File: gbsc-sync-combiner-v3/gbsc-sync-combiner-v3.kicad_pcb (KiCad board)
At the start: 2 copper layers, 33 x 48 mm, 14 parts, among them J1 DB15_Female_HighDensity_Mount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, J2 JST-XH, J3 JST-XH, U1 74LS86

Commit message: minor adjustment
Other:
- board text added: "GBS-C Sync Combiner v1.3 c. 01/2022 Details on Github: Softdrink117/gbsc-sync-combiner CERN-OHL-W"
- board text removed: "GBS-C Sync Combiner v1.0 c. 11/2021 Details on Github: Softdrink117/gbsc-sync-combiner CERN-OHL-W"
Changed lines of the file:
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@@
     (effects (font (size 0.4572 0.4572) (thickness 0.0762)) (justify left))
   )
-  (gr_text "GBS-C Sync Combiner \nv1.0 c. 11/2021\nDetails on Github:\nSoftdrink117/gbsc-sync-combiner\nCERN-OHL-W" (at 109.5 93) (layer "F.SilkS")
+  (gr_text "GBS-C Sync Combiner \nv1.3 c. 01/2022\nDetails on Github:\nSoftdrink117/gbsc-sync-combiner\nCERN-OHL-W" (at 109.5 93) (layer "F.SilkS")
     (effects (font (size 0.4572 0.4572) (thickness 0.0762)) (justify left))
   )
@@
   )
   (segment (start 109.793312 81.043312) (end 117.293312 73.543312) (width 0.381) (layer "F.Cu") (net 1))
-  (segment (start 107 64.75) (end 107 62) (width 0.381) (layer "F.Cu") (net 1))
   (segment (start 110 87) (end 117.396447 87) (width 0.381) (layer "F.Cu") (net 1))
   (segment (start 108.362605 79.194999) (end 102.906659 79.194999) (width 0.381) (layer "F.Cu") (net 1))
@@
   (segment (start 121.644511 72.144511) (end 121.644511 56.644511) (width 0.381) (layer "F.Cu") (net 1))
   (segment (start 110 61.5) (end 110 59) (width 0.381) (layer "F.Cu") (net 1))
+  (segment (start 107 64.75) (end 107 62.75) (width 0.381) (layer "F.Cu") (net 1))
   (segment (start 102.10666 76.105) (end 102.10666 78.395) (width 0.381) (layer "F.Cu") (net 1))
   (segment (start 110.916833 61.5) (end 110 61.5) (width 0.381) (layer "F.Cu") (net 1))
   (segment (start 118.603553 87.5) (end 120 87.5) (width 0.381) (layer "F.Cu") (net 1))
-  (segment (start 107.5 61.5) (end 110 61.5) (width 0.381) (layer "F.Cu") (net 1))
   (segment (start 120 84.24) (end 120 87.5) (width 0.381) (layer "F.Cu") (net 1))
   (segment (start 111.505971 61.744029) (end 117.421136 67.659194) (width 0.381) (layer "F.Cu") (net 1))
@@
   (segment (start 108.60949 85.057226) (end 108.60949 83.14051) (width 0.381) (layer "F.Cu") (net 1))
   (segment (start 102.10666 73.815) (end 102.10666 76.105) (width 0.381) (layer "F.Cu") (net 1))
+  (segment (start 108.25 61.5) (end 110 61.5) (width 0.381) (layer "F.Cu") (net 1))
   (segment (start 110 55.853553) (end 110 59) (width 0.381) (layer "F.Cu") (net 1))
   (segment (start 118.871756 72.889499) (end 120.899523 72.889499) (width 0.381) (layer "F.Cu") (net 1))
@@
   (arc (start 109.75 55.25) (mid 109.935027 55.526912) (end 110 55.853553) (width 0.381) (layer "F.Cu") (net 1))
   (arc (start 109 86) (mid 108.710981 85.567452) (end 108.60949 85.057226) (width 0.381) (layer "F.Cu") (net 1))
-  (arc (start 107 62) (mid 107.146447 61.646447) (end 107.5 61.5) (width 0.381) (layer "F.Cu") (net 1))
   (arc (start 110.36541 78.36541) (mid 109.446515 78.979396) (end 108.362605 79.194999) (width 0.381) (layer "F.Cu") (net 1))
+  (arc (start 107 62.75) (mid 107.366117 61.866117) (end 108.25 61.5) (width 0.381) (layer "F.Cu") (net 1))
   (arc (start 117.293312 73.543312) (mid 118.017507 73.05942) (end 118.871756 72.889499) (width 0.381) (layer "F.Cu") (net 1))
   (segment (start 127.62 71.54) (end 127.62 74.08) (width 0.381) (layer "F.Cu") (net 2))
@@
   (arc (start 105.896447 77.25) (mid 106.223087 77.185028) (end 106.5 77) (width 0.254) (layer "F.Cu") (net 13))
   (arc (start 106.5 77) (mid 107.053825 76.629946) (end 107.707106 76.5) (width 0.254) (layer "F.Cu") (net 13))
-  (segment (start 115.103553 68.5) (end 116.5 68.5) (width 0.254) (layer "F.Cu") (net 15))
-  (segment (start 110 69) (end 113.896447 69) (width 0.254) (layer "F.Cu") (net 15))
-  (arc (start 114.5 68.75) (mid 114.776912 68.564973) (end 115.103553 68.5) (width 0.254) (layer "F.Cu") (net 15))
-  (arc (start 113.896447 69) (mid 114.223087 68.935028) (end 114.5 68.75) (width 0.254) (layer "F.Cu") (net 15))
+  (segment (start 113.103553 68.5) (end 116.5 68.5) (width 0.254) (layer "F.Cu") (net 15))
+  (segment (start 110 69) (end 111.896447 69) (width 0.254) (layer "F.Cu") (net 15))
+  (arc (start 112.5 68.75) (mid 112.776912 68.564973) (end 113.103553 68.5) (width 0.254) (layer "F.Cu") (net 15))
+  (arc (start 111.896447 69) (mid 112.223087 68.935028) (end 112.5 68.75) (width 0.254) (layer "F.Cu") (net 15))
   (segment (start 116.5 80.25) (end 116.5 78.66) (width 0.254) (layer "F.Cu") (net 16))
   (segment (start 120 81.7) (end 117.95 81.7) (width 0.254) (layer "F.Cu") (net 16))

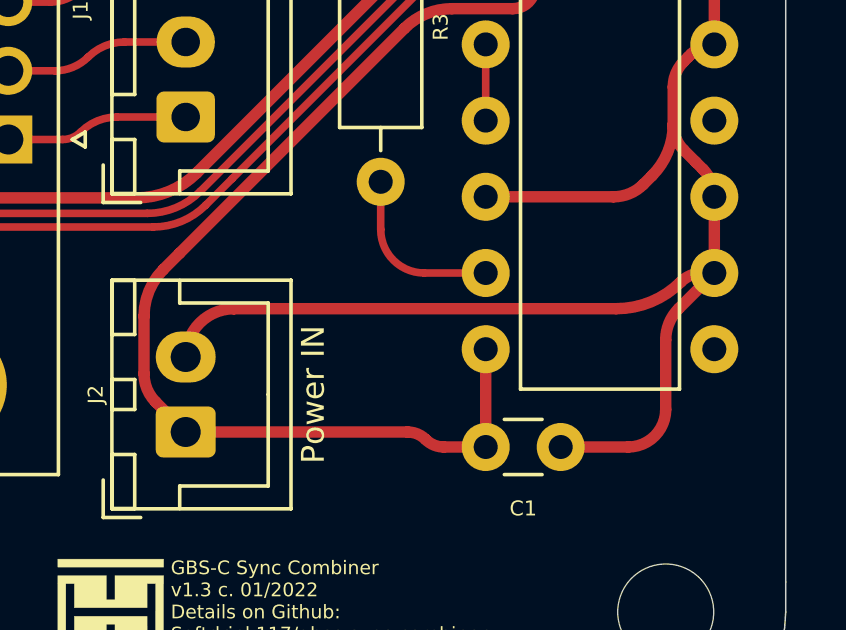
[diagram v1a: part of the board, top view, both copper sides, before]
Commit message: Edited gitignore, minor board adjustments
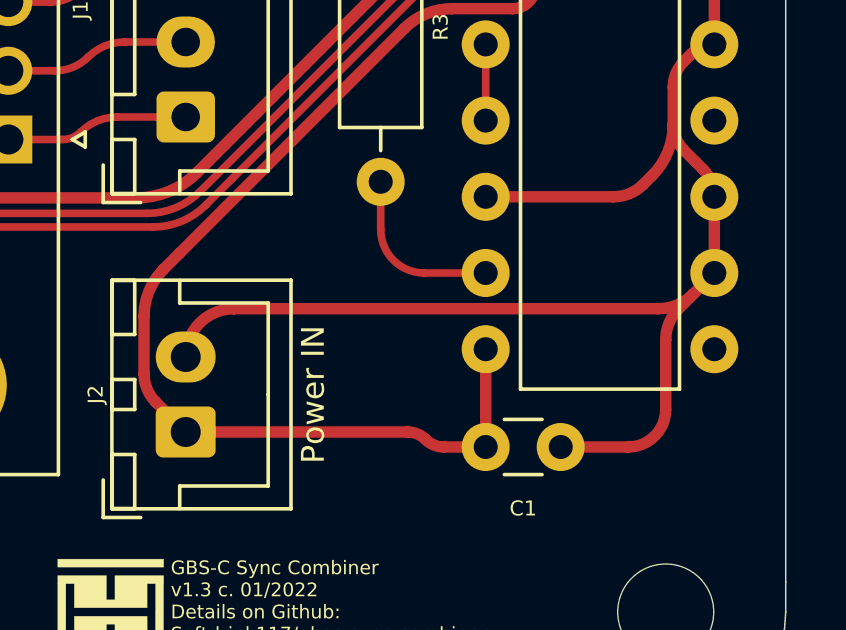
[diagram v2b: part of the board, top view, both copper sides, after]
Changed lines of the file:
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@@
   (segment (start 127.62 71.54) (end 127.62 74.08) (width 0.381) (layer "F.Cu") (net 2))
   (segment (start 126.603553 74.646446) (end 126.75 74.5) (width 0.381) (layer "F.Cu") (net 2))
-  (segment (start 127.62 81.7) (end 126.429499 82.890501) (width 0.381) (layer "F.Cu") (net 2))
   (segment (start 127 78) (end 126.603554 77.603554) (width 0.381) (layer "F.Cu") (net 2))
   (segment (start 127.66 58.5) (end 127.66 62.5) (width 0.381) (layer "F.Cu") (net 2))
@@
   (segment (start 122.5 87.5) (end 124.75 87.5) (width 0.381) (layer "F.Cu") (net 2))
   (segment (start 120 79.16) (end 124.260173 79.16) (width 0.381) (layer "F.Cu") (net 2))
+  (segment (start 111.609499 82.890501) (end 111.609989 82.890011) (width 0.381) (layer "F.Cu") (net 2))
   (segment (start 127.66 68.96) (end 127.62 69) (width 0.381) (layer "F.Cu") (net 2))
   (segment (start 127.224264 81.7) (end 127.62 81.7) (width 0.381) (layer "F.Cu") (net 2))
+  (segment (start 127.62 81.7) (end 126.91 82.41) (width 0.381) (layer "F.Cu") (net 2))
   (segment (start 126.75 74.5) (end 126.851801 74.398199) (width 0.381) (layer "F.Cu") (net 2))
+  (segment (start 111.609989 82.890011) (end 125.751151 82.890011) (width 0.381) (layer "F.Cu") (net 2))
   (segment (start 126.25 76.75) (end 126.25 75.5) (width 0.381) (layer "F.Cu") (net 2))
-  (segment (start 111.609989 82.890011) (end 124.351324 82.890011) (width 0.381) (layer "F.Cu") (net 2))
+  (segment (start 126.91 82.41) (end 126.429499 82.890501) (width 0.381) (layer "F.Cu") (net 2))
   (segment (start 127.62 79.16) (end 127.62 81.7) (width 0.381) (layer "F.Cu") (net 2))
   (segment (start 127.238162 78.238163) (end 127 78) (width 0.381) (layer "F.Cu") (net 2))
-  (segment (start 111.609499 82.890501) (end 111.609989 82.890011) (width 0.381) (layer "F.Cu") (net 2))
   (segment (start 125.25 78.75) (end 125.542893 78.457107) (width 0.381) (layer "F.Cu") (net 2))
   (segment (start 127.66 62.5) (end 127.66 68.96) (width 0.381) (layer "F.Cu") (net 2))
-  (arc (start 111.609499 82.890501) (mid 110.471411 83.361912) (end 110 84.5) (width 0.381) (layer "F.Cu") (net 2))
   (arc (start 126.851801 74.398199) (mid 127.204253 74.162698) (end 127.62 74.08) (width 0.381) (layer "F.Cu") (net 2))
   (arc (start 126 83.927403) (mid 126.111623 83.366236) (end 126.429499 82.890501) (width 0.381) (layer "F.Cu") (net 2))
+  (arc (start 125.751151 82.890011) (mid 126.378315 82.765261) (end 126.91 82.41) (width 0.381) (layer "F.Cu") (net 2))
   (arc (start 126.603554 77.603554) (mid 126.341886 77.21194) (end 126.25 76.75) (width 0.381) (layer "F.Cu") (net 2))
+  (arc (start 110 84.5) (mid 110.471411 83.361912) (end 111.609499 82.890501) (width 0.381) (layer "F.Cu") (net 2))
   (arc (start 127.62 79.16) (mid 127.520764 78.661105) (end 127.238162 78.238163) (width 0.381) (layer "F.Cu") (net 2))
   (arc (start 126.25 75.5) (mid 126.341886 75.03806) (end 126.603553 74.646446) (width 0.381) (layer "F.Cu") (net 2))
   (arc (start 124.260173 79.16) (mid 124.795863 79.053445) (end 125.25 78.75) (width 0.381) (layer "F.Cu") (net 2))
-  (arc (start 126.5 82) (mid 126.832294 81.777968) (end 127.224264 81.7) (width 0.381) (layer "F.Cu") (net 2))
   (arc (start 124.75 87.5) (mid 125.633883 87.133883) (end 126 86.25) (width 0.381) (layer "F.Cu") (net 2))
   (arc (start 125.542893 78.457107) (mid 126.066229 77.67388) (end 126.25 76.75) (width 0.381) (layer "F.Cu") (net 2))
-  (arc (start 124.351324 82.890011) (mid 125.514179 82.658705) (end 126.5 82) (width 0.381) (layer "F.Cu") (net 2))
   (arc (start 127.54 74) (mid 127.596569 74.023431) (end 127.62 74.08) (width 0.381) (layer "F.Cu") (net 2))
   (segment (start 102.03666 60.435) (end 97.873593 64.598067) (width 0.381) (layer "F.Cu") (net 3))

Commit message: Major updates
- Updated v1.3 PCB design
- Created README
- Created BOM
- Created gerbers
- Sent gerbers to fab
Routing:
- net /HSync: track 46.6 -> 45.1 mm
- net +5V: track 59.8 -> 59.2 mm
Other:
- board text added: "GBS-C Sync Combiner v1.3 c. 01/2022 Design by Softdrink 117 Details on Github: Softdrink117/gbsc-sync-combiner"
- board text removed: "GBS-C Sync Combiner v1.3 c. 01/2022 Details on Github: Softdrink117/gbsc-sync-combiner CERN-OHL-W"
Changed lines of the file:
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@@
     (pad_to_mask_clearance 0)
     (pcbplotparams
-      (layerselection 0x00010fc_ffffffff)
+      (layerselection 0x00010f0_ffffffff)
       (disableapertmacros false)
       (usegerberextensions false)
@@
       (outputformat 1)
       (mirror false)
-      (drillshape 1)
+      (drillshape 0)
       (scaleselection 1)
-      (outputdirectory "")
+      (outputdirectory "gerber/")
     )
   )
@@
     (fp_line (start -2.45 -2.35) (end -2.45 3.4) (layer "F.Fab") (width 0.1))
     (fp_line (start -0.625 -2.35) (end 0 -1.35) (layer "F.Fab") (width 0.1))
-    (pad "1" thru_hole roundrect locked (at 0 0 90) (size 1.7 2) (drill 1) (layers *.Cu *.Mask) (roundrect_rratio 0.147059)
+    (pad "1" thru_hole roundrect locked (at 0 0 90) (size 1.7 2) (drill 1) (layers *.Cu *.Mask) (roundrect_rratio 0.1470588235)
       (net 1 "GND"))
     (pad "2" thru_hole oval locked (at 2.5 0 90) (size 1.7 2) (drill 1) (layers *.Cu *.Mask)
@@
     (fp_line (start 19.95 -2.35) (end -2.45 -2.35) (layer "F.Fab") (width 0.1))
     (fp_line (start -2.45 3.4) (end 19.95 3.4) (layer "F.Fab") (width 0.1))
-    (pad "1" thru_hole roundrect locked (at 0 0 90) (size 1.7 1.95) (drill 0.95) (layers *.Cu *.Mask) (roundrect_rratio 0.147059)
+    (pad "1" thru_hole roundrect locked (at 0 0 90) (size 1.7 1.95) (drill 0.95) (layers *.Cu *.Mask) (roundrect_rratio 0.1470588235)
       (net 13 "Red"))
     (pad "2" thru_hole oval locked (at 2.5 0 90) (size 1.7 1.95) (drill 0.95) (layers *.Cu *.Mask)
@@
   (gr_poly
     (pts
-      (xy 109.5 54)
-      (xy 108.5 54)
-      (xy 108.5 53)
-      (xy 109.5 53)
+      (xy 109.05 54)
+      (xy 108.6 54)
+      (xy 108.6 53)
+      (xy 109.05 53)
     ) (layer "F.Mask") (width 0.1) (fill solid))
   (gr_line (start 101 49) (end 102 49) (layer "Edge.Cuts") (width 0.05))
@@
     (effects (font (size 0.4572 0.4572) (thickness 0.0762)) (justify left))
   )
-  (gr_text "GBS-C Sync Combiner \nv1.3 c. 01/2022\nDetails on Github:\nSoftdrink117/gbsc-sync-combiner\nCERN-OHL-W" (at 109.5 93) (layer "F.SilkS")
+  (gr_text "GBS-C Sync Combiner \nv1.3 c. 01/2022\nDesign by Softdrink 117\nDetails on Github:\nSoftdrink117/gbsc-sync-combiner" (at 109.50001 92.999992) (layer "F.SilkS")
     (effects (font (size 0.4572 0.4572) (thickness 0.0762)) (justify left))
   )
@@
   (segment (start 111.609499 82.890501) (end 111.609989 82.890011) (width 0.381) (layer "F.Cu") (net 2))
   (segment (start 127.66 68.96) (end 127.62 69) (width 0.381) (layer "F.Cu") (net 2))
-  (segment (start 127.224264 81.7) (end 127.62 81.7) (width 0.381) (layer "F.Cu") (net 2))
   (segment (start 127.62 81.7) (end 126.91 82.41) (width 0.381) (layer "F.Cu") (net 2))
   (segment (start 126.75 74.5) (end 126.851801 74.398199) (width 0.381) (layer "F.Cu") (net 2))
@@
   (arc (start 124.75 87.5) (mid 125.633883 87.133883) (end 126 86.25) (width 0.381) (layer "F.Cu") (net 2))
   (arc (start 125.542893 78.457107) (mid 126.066229 77.67388) (end 126.25 76.75) (width 0.381) (layer "F.Cu") (net 2))
-  (arc (start 127.54 74) (mid 127.596569 74.023431) (end 127.62 74.08) (width 0.381) (layer "F.Cu") (net 2))
   (segment (start 102.03666 60.435) (end 97.873593 64.598067) (width 0.381) (layer "F.Cu") (net 3))
-  (segment (start 102.03666 85.435) (end 101.935 85.435) (width 0.381) (layer "F.Cu") (net 3))
   (segment (start 97.5 65.5) (end 97.5 80.792894) (width 0.381) (layer "F.Cu") (net 3))
   (segment (start 102.03666 60.435) (end 107.654354 54.817306) (width 0.381) (layer "F.Cu") (net 3))
   (segment (start 98 82) (end 101.009562 85.009562) (width 0.381) (layer "F.Cu") (net 3))
-  (arc (start 102.01662 60.48338) (mid 102.031452 60.461183) (end 102.03666 60.435) (width 0.381) (layer "F.Cu") (net 3))
   (arc (start 107.654354 54.817306) (mid 108.058191 54.212922) (end 108.2 53.5) (width 0.381) (layer "F.Cu") (net 3))
   (arc (start 97.873593 64.598067) (mid 97.597094 65.011877) (end 97.5 65.5) (width 0.381) (layer "F.Cu") (net 3))
@@
   (segment (start 116 64.43934) (end 116 64.25) (width 0.254) (layer "F.Cu") (net 6))
   (segment (start 118.246905 68.246905) (end 118.246905 69.003095) (width 0.254) (layer "F.Cu") (net 6))
-  (segment (start 120 69) (end 119.5 69) (width 0.254) (layer "F.Cu") (net 6))
   (segment (start 118.246905 70.746905) (end 118.246905 69.003095) (width 0.254) (layer "F.Cu") (net 6))
-  (segment (start 120 69) (end 120 69.462689) (width 0.254) (layer "F.Cu") (net 6))
   (segment (start 110.481344 78.981344) (end 117.915358 71.54733) (width 0.254) (layer "F.Cu") (net 6))
   (segment (start 98.82056 73.9761) (end 100.12666 72.67) (width 0.254) (layer "F.Cu") (net 6))
@@
   (segment (start 118.246905 69.003095) (end 119.996905 69.003095) (width 0.254) (layer "F.Cu") (net 6))
   (segment (start 116 60.53033) (end 116 64.25) (width 0.254) (layer "F.Cu") (net 6))
-  (segment (start 120 69) (end 119.49381 69) (width 0.254) (layer "F.Cu") (net 6))
   (segment (start 99.5 78.5) (end 98.853554 77.853554) (width 0.254) (layer "F.Cu") (net 6))
   (arc (start 117.893351 67.393351) (mid 118.155019 67.784965) (end 118.246905 68.246905) (width 0.254) (layer "F.Cu") (net 6))
